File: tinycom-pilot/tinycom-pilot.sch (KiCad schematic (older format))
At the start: 31 parts, among them J1 MICRO_SD_HINGE, P1 CONN_02X08, P2 CONN_02X08, P3 USB_A, P4 USB_OTG, U1 SY8008BAAC, U2 SY8008BAAC, U3 SY8008BAAC, U4 RTL8723BS(ComboModule)

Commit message: pilot pic
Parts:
- removed C12: CP_Small, Capacitors_Elko_ThroughHole:Elko_vert_11.2x6.3mm_RM2.5_CopperClear, symbol CP_Small
- removed HDMI1: HDMI-SWM-19, tinycom:HDMI-SWM-19, symbol HDMI-SWM-19
- removed P4: USB_OTG, tinycom:tc-USB_Micro-B, symbol USB_OTG
- removed U4: RTL8723BS(ComboModule), tinycom:RL-SM02BD(RTL8723BS), symbol RTL8723BS(ComboModule)
- added U4: conn-3x10, tinycom:Pin_Header_Angled_3x10, symbol conn-3x10
- added U5: STM32-48PIN, Housings_QFP:LQFP-48_7x7mm_Pitch0.5mm, symbol STM32-48PIN
- added U6: MPU6050, Housings_DFN_QFN:QFN-24-1EP_4x4mm_Pitch0.5mm, symbol MPU6050
- added U7: MS6511, tinycom:ms5611, symbol MS6511
- C11: footprint Capacitors_Elko_ThroughHole:Elko_vert_11.2x6.3mm_RM2.5_CopperClear -> Capacitors_Tantalum_SMD:TantalC_SizeT_EIA-3528
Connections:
- wire segments 118 -> 108
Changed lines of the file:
@@
 LIBS:tinycom
 LIBS:hdmi-swm-19
-LIBS:tinycom-wifi-cache
+LIBS:conn-3x10
+LIBS:tinycom-pilot-cache
 EELAYER 25 0
 EELAYER END
@@
 $EndComp
 $Comp
-L +5V #PWR14
-U 1 1 562DA8F7
-P 5250 4200
-F 0 "#PWR14" H 5250 4050 50  0001 C CNN
-F 1 "+5V" H 5250 4340 50  0000 C CNN
-F 2 "" H 5250 4200 60  0000 C CNN
-F 3 "" H 5250 4200 60  0000 C CNN
-	1    5250 4200
-	1    0    0    -1
-$EndComp
-$Comp
-L GND #PWR15
-U 1 1 562DA928
-P 5250 4600
-F 0 "#PWR15" H 5250 4350 50  0001 C CNN
-F 1 "GND" H 5250 4450 50  0000 C CNN
-F 2 "" H 5250 4600 60  0000 C CNN
-F 3 "" H 5250 4600 60  0000 C CNN
-	1    5250 4600
-	1    0    0    -1
-$EndComp
-Text GLabel 5450 4350 0    60   Input ~ 0
-UDM0
-Text GLabel 5450 4450 0    60   Input ~ 0
-UDP0
-$Comp
-L +5V #PWR16
+L +5V #PWR01
 U 1 1 562DAC42
 P 5300 5050
-F 0 "#PWR16" H 5300 4900 50  0001 C CNN
+F 0 "#PWR01" H 5300 4900 50  0001 C CNN
 F 1 "+5V" H 5300 5190 50  0000 C CNN
 F 2 "" H 5300 5050 60  0000 C CNN
@@
 $EndComp
 $Comp
-L GND #PWR17
+L GND #PWR02
 U 1 1 562DAC77
 P 5300 5500
-F 0 "#PWR17" H 5300 5250 50  0001 C CNN
+F 0 "#PWR02" H 5300 5250 50  0001 C CNN
 F 1 "GND" H 5300 5350 50  0000 C CNN
 F 2 "" H 5300 5500 60  0000 C CNN
@@
 UDP1
 $Comp
-L GND #PWR5
+L GND #PWR03
 U 1 1 562DAF0B
 P 1350 1750
-F 0 "#PWR5" H 1350 1500 50  0001 C CNN
+F 0 "#PWR03" H 1350 1500 50  0001 C CNN
 F 1 "GND" H 1350 1600 50  0000 C CNN
 F 2 "" H 1350 1750 60  0000 C CNN
@@
 $EndComp
 $Comp
-L +5V #PWR3
+L +5V #PWR04
 U 1 1 562DAF87
 P 1250 1350
-F 0 "#PWR3" H 1250 1200 50  0001 C CNN
+F 0 "#PWR04" H 1250 1200 50  0001 C CNN
 F 1 "+5V" H 1250 1490 50  0000 C CNN
 F 2 "" H 1250 1350 60  0000 C CNN
@@
 $EndComp
 $Comp
-L +5V #PWR1
+L +5V #PWR05
 U 1 1 562DB0A5
 P 1150 2550
-F 0 "#PWR1" H 1150 2400 50  0001 C CNN
+F 0 "#PWR05" H 1150 2400 50  0001 C CNN
 F 1 "+5V" H 1150 2690 50  0000 C CNN
 F 2 "" H 1150 2550 60  0000 C CNN
@@
 $EndComp
 $Comp
-L GND #PWR6
+L GND #PWR06
 U 1 1 562DB1B7
 P 1350 2900
-F 0 "#PWR6" H 1350 2650 50  0001 C CNN
+F 0 "#PWR06" H 1350 2650 50  0001 C CNN
 F 1 "GND" H 1350 2750 50  0000 C CNN
 F 2 "" H 1350 2900 60  0000 C CNN
@@
 $EndComp
 $Comp
-L +5V #PWR2
+L +5V #PWR07
 U 1 1 562DB2B7
 P 1150 3800
-F 0 "#PWR2" H 1150 3650 50  0001 C CNN
+F 0 "#PWR07" H 1150 3650 50  0001 C CNN
 F 1 "+5V" H 1150 3940 50  0000 C CNN
 F 2 "" H 1150 3800 60  0000 C CNN
@@
 $EndComp
 $Comp
-L GND #PWR4
+L GND #PWR08
 U 1 1 562DB346
 P 1300 4150
-F 0 "#PWR4" H 1300 3900 50  0001 C CNN
+F 0 "#PWR08" H 1300 3900 50  0001 C CNN
 F 1 "GND" H 1300 4000 50  0000 C CNN
 F 2 "" H 1300 4150 60  0000 C CNN
@@
 VCC_15
 $Comp
-L GND #PWR19
+L GND #PWR09
 U 1 1 562DAEC4
 P 7450 2400
-F 0 "#PWR19" H 7450 2150 50  0001 C CNN
+F 0 "#PWR09" H 7450 2150 50  0001 C CNN
 F 1 "GND" H 7450 2250 50  0000 C CNN
 F 2 "" H 7450 2400 60  0000 C CNN
@@
 $EndComp
 $Comp
-L GND #PWR21
+L GND #PWR010
 U 1 1 562DA997
 P 8650 2450
-F 0 "#PWR21" H 8650 2200 50  0001 C CNN
+F 0 "#PWR010" H 8650 2200 50  0001 C CNN
 F 1 "GND" H 8650 2300 50  0000 C CNN
 F 2 "" H 8650 2450 60  0000 C CNN
@@
 SDC0_D1
 $Comp
-L GND #PWR20
+L GND #PWR011
 U 1 1 562DAEE9
 P 7450 4950
-F 0 "#PWR20" H 7450 4700 50  0001 C CNN
+F 0 "#PWR011" H 7450 4700 50  0001 C CNN
 F 1 "GND" H 7450 4800 50  0000 C CNN
 F 2 "" H 7450 4950 60  0000 C CNN
@@
 $EndComp
 $Comp
-L GND #PWR22
+L GND #PWR012
 U 1 1 562DAF47
 P 9050 5450
-F 0 "#PWR22" H 9050 5200 50  0001 C CNN
+F 0 "#PWR012" H 9050 5200 50  0001 C CNN
 F 1 "GND" H 9050 5300 50  0000 C CNN
 F 2 "" H 9050 5450 60  0000 C CNN
@@
 $EndComp
 $Comp
-L +3.3V #PWR18
+L +3.3V #PWR013
 U 1 1 562DB369
 P 7300 4000
-F 0 "#PWR18" H 7300 3850 50  0001 C CNN
+F 0 "#PWR013" H 7300 3850 50  0001 C CNN
 F 1 "+3.3V" H 7300 4140 50  0000 C CNN
 F 2 "" H 7300 4000 60  0000 C CNN
@@
 $EndComp
 $Comp
-L GND #PWR9
+L GND #PWR014
 U 1 1 562DB89F
 P 3250 2000
-F 0 "#PWR9" H 3250 1750 50  0001 C CNN
+F 0 "#PWR014" H 3250 1750 50  0001 C CNN
 F 1 "GND" H 3250 1850 50  0000 C CNN
 F 2 "" H 3250 2000 60  0000 C CNN
@@
 $EndComp
 $Comp
-L +3.3V #PWR10
+L +3.3V #PWR015
 U 1 1 562DBC47
 P 3600 1350
-F 0 "#PWR10" H 3600 1200 50  0001 C CNN
+F 0 "#PWR015" H 3600 1200 50  0001 C CNN
 F 1 "+3.3V" H 3600 1490 50  0000 C CNN
 F 2 "" H 3600 1350 60  0000 C CNN
@@
 $EndComp
 $Comp
-L GND #PWR8
+L GND #PWR016
 U 1 1 562F8BF0
 P 3150 3150
-F 0 "#PWR8" H 3150 2900 50  0001 C CNN
+F 0 "#PWR016" H 3150 2900 50  0001 C CNN
 F 1 "GND" H 3150 3000 50  0000 C CNN
 F 2 "" H 3150 3150 60  0000 C CNN
@@
 $EndComp
 $Comp
-L GND #PWR7
+L GND #PWR017
 U 1 1 562F9FD4
 P 3100 4550
-F 0 "#PWR7" H 3100 4300 50  0001 C CNN
+F 0 "#PWR017" H 3100 4300 50  0001 C CNN
 F 1 "GND" H 3100 4400 50  0000 C CNN
 F 2 "" H 3100 4550 60  0000 C CNN
@@
 $EndComp
 $Comp
-L GND #PWR11
+L GND #PWR018
 U 1 1 56336272
 P 4400 1900
-F 0 "#PWR11" H 4400 1650 50  0001 C CNN
+F 0 "#PWR018" H 4400 1650 50  0001 C CNN
 F 1 "GND" H 4400 1750 50  0000 C CNN
 F 2 "" H 4400 1900 60  0000 C CNN
@@
 $EndComp
 $Comp
-L GND #PWR12
-U 1 1 5634B03F
-P 4900 4550
-F 0 "#PWR12" H 4900 4300 50  0001 C CNN
-F 1 "GND" H 4900 4400 50  0000 C CNN
-F 2 "" H 4900 4550 60  0000 C CNN
-F 3 "" H 4900 4550 60  0000 C CNN
-	1    4900 4550
-	1    0    0    -1
-$EndComp
-$Comp
-L GND #PWR13
+L GND #PWR019
 U 1 1 5634B0B0
 P 4900 5400
-F 0 "#PWR13" H 4900 5150 50  0001 C CNN
+F 0 "#PWR019" H 4900 5150 50  0001 C CNN
 F 1 "GND" H 4900 5250 50  0000 C CNN
 F 2 "" H 4900 5400 60  0000 C CNN
 F 3 "" H 4900 5400 60  0000 C CNN
 	1    4900 5400
-	1    0    0    -1
-$EndComp
-$Comp
-L CP_Small C11
-U 1 1 5634BEB9
-P 4600 5250
-F 0 "C11" H 4610 5320 50  0000 L CNN
-F 1 "CP_Small" H 4610 5170 50  0000 L CNN
-F 2 "Capacitors_Elko_ThroughHole:Elko_vert_11.2x6.3mm_RM2.5_CopperClear" H 4600 5250 60  0001 C CNN
-F 3 "" H 4600 5250 60  0000 C CNN
-	1    4600 5250
-	1    0    0    -1
-$EndComp
-$Comp
-L CP_Small C12
-U 1 1 5634C85E
-P 4650 4400
-F 0 "C12" H 4660 4470 50  0000 L CNN
-F 1 "CP_Small" H 4660 4320 50  0000 L CNN
-F 2 "Capacitors_Elko_ThroughHole:Elko_vert_11.2x6.3mm_RM2.5_CopperClear" H 4650 4400 60  0001 C CNN
-F 3 "" H 4650 4400 60  0000 C CNN
-	1    4650 4400
 	1    0    0    -1
 $EndComp
@@
 NoConn ~ 6800 2550
 NoConn ~ 6800 2650
-$Comp
-L USB_OTG P4
-U 1 1 565013FA
-P 5750 4450
-F 0 "P4" H 6075 4325 50  0000 C CNN
-F 1 "USB_OTG" H 5750 4650 50  0000 C CNN
-F 2 "tinycom:tc-USB_Micro-B" V 5700 4350 60  0000 C CNN
-F 3 "" V 5700 4350 60  0000 C CNN
-	1    5750 4450
-	0    1    1    0
-$EndComp
-Wire Wire Line
-	4650 4250 5450 4250
-Wire Wire Line
-	5250 4250 5250 4200
-Wire Wire Line
-	5450 4550 5250 4550
-Wire Wire Line
-	5250 4550 5250 4600
 Wire Wire Line
 	4600 5100 5450 5100
@@
 	4900 5350 4900 5400
 Wire Wire Line
-	4900 4500 4900 4550
-Connection ~ 5250 4250
-Wire Wire Line
-	4650 4250 4650 4300
-Wire Wire Line
-	4650 4500 4900 4500
-Wire Wire Line
 	4600 5100 4600 5150
 Wire Wire Line
@@
 Wire Wire Line
 	7200 4850 7450 4850
-Wire Wire Line
-	5450 4650 5350 4650
-Wire Wire Line
-	5350 4550 5350 4850
-Connection ~ 5350 4550
-Wire Wire Line
-	5350 4850 5850 4850
-Connection ~ 5350 4650
-$Comp
-L RTL8723BS(ComboModule) U4
-U 1 1 56591901
-P 2000 6200
-F 0 "U4" H 1600 7575 60  0000 C CNN
-F 1 "RTL8723BS(ComboModule)" H 2000 4825 60  0000 C CNN
-F 2 "tinycom:RL-SM02BD(RTL8723BS)" H 2000 6000 60  0000 C CNN
-F 3 "" H 2000 6000 60  0000 C CNN
-	1    2000 6200
-	1    0    0    -1
-$EndComp
 Wire Wire Line
 	7950 3950 7950 4750
@@
 	8250 3850 8250 4000
 $Comp
-L HDMI-SWM-19 HDMI1
-U 1 1 56591D96
-P 3450 6150
-F 0 "HDMI1" H 3550 7150 50  0000 L BNN
-F 1 "HDMI-SWM-19" H 3550 5050 50  0000 L BNN
-F 2 "tinycom:HDMI-SWM-19" H 3480 6300 20  0001 C CNN
-F 3 "" H 3450 6150 60  0000 C CNN
-	1    3450 6150
-	1    0    0    -1
-$EndComp
+L conn-3x10 U4
+U 1 1 56594134
+P 1750 5350
+F 0 "U4" H 1750 5350 60  0000 C CNN
+F 1 "conn-3x10" H 1750 5350 60  0000 C CNN
+F 2 "tinycom:Pin_Header_Angled_3x10" H 1750 5350 60  0000 C CNN
+F 3 "" H 1750 5350 60  0000 C CNN
+	1    1750 5350
+	1    0    0    -1
+$EndComp
+$Comp
+L STM32-48PIN U5
+U 1 1 5659585F
+P 3350 7350
+F 0 "U5" H 2350 9100 60  0000 C CNN
+F 1 "STM32-48PIN" H 2600 5550 60  0000 C CNN
+F 2 "Housings_QFP:LQFP-48_7x7mm_Pitch0.5mm" H 3350 7350 60  0000 C CNN
+F 3 "" H 3350 7350 60  0000 C CNN
+	1    3350 7350
+	1    0    0    -1
+$EndComp
+$Comp
+L CP_Small C11
+U 1 1 5634BEB9
+P 4600 5250
+F 0 "C11" H 4610 5320 50  0000 L CNN
+F 1 "CP_Small" H 4610 5170 50  0000 L CNN
+F 2 "Capacitors_Tantalum_SMD:TantalC_SizeT_EIA-3528" H 4600 5250 60  0001 C CNN
+F 3 "" H 4600 5250 60  0000 C CNN
+	1    4600 5250
+	1    0    0    -1
+$EndComp
+$Comp
+L MPU6050 U6
+U 1 1 5659749B
+P 8600 1350
+F 0 "U6" H 8550 1450 60  0000 C CNN
+F 1 "MPU6050" H 8550 1450 60  0000 C CNN
+F 2 "Housings_DFN_QFN:QFN-24-1EP_4x4mm_Pitch0.5mm" H 8550 1450 60  0000 C CNN
+F 3 "" H 8550 1450 60  0000 C CNN
+	1    8600 1350
+	1    0    0    -1
+$EndComp
+$Comp
+L MS6511 U7
+U 1 1 56597816
+P 10000 1050
+F 0 "U7" H 10000 1050 60  0000 C CNN
+F 1 "MS6511" H 10000 1050 60  0000 C CNN
+F 2 "tinycom:ms5611" H 10000 1050 60  0000 C CNN
+F 3 "" H 10000 1050 60  0000 C CNN
+	1    10000 1050
+	1    0    0    -1
+$EndComp

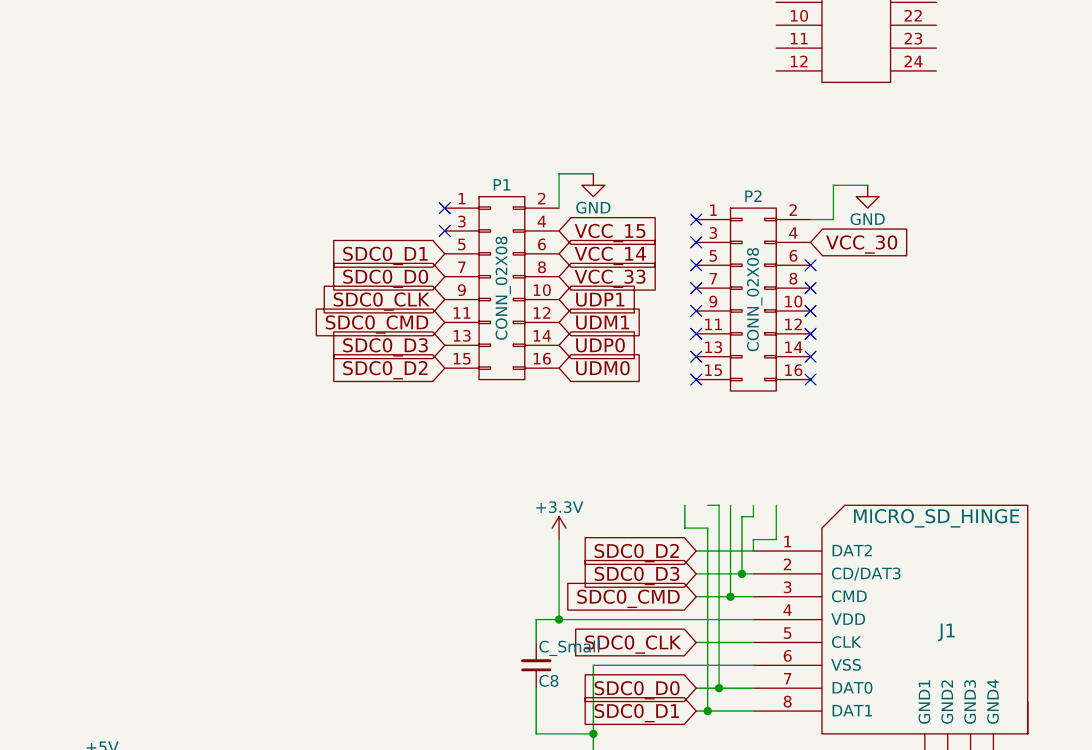
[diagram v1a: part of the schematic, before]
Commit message: change connectors
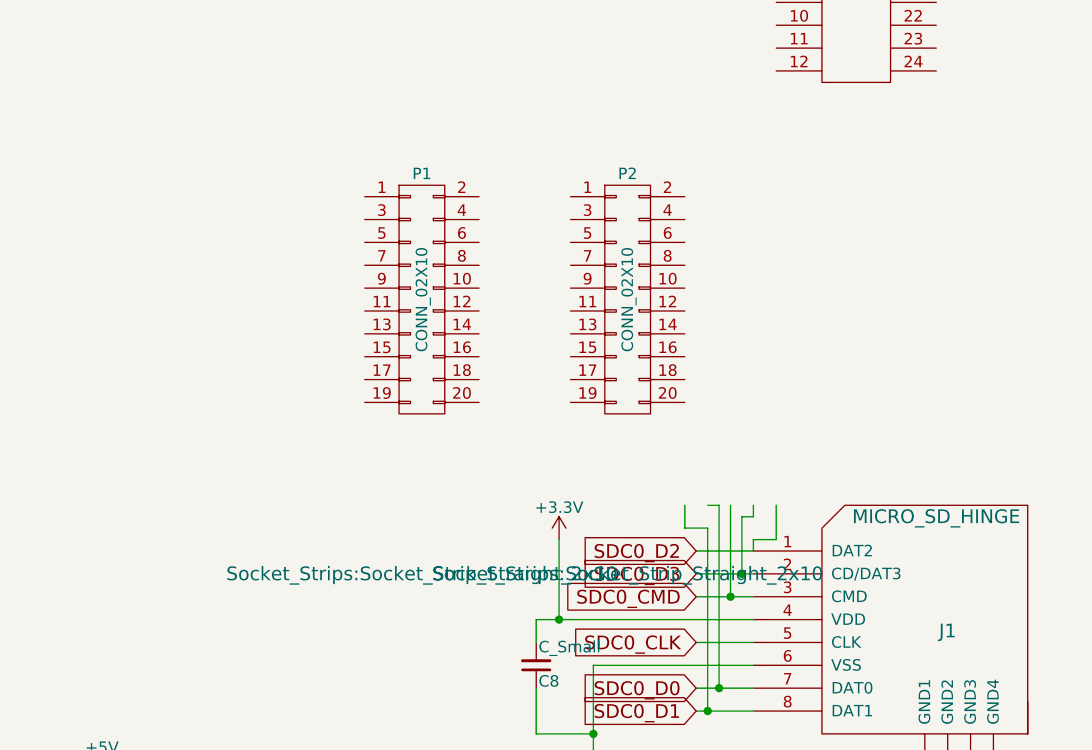
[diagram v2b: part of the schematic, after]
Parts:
- removed P1, P2: CONN_02X08, Socket_Strips:Socket_Strip_Straight_2x08, symbol CONN_02X08
- added P1, P2: CONN_02X10, Socket_Strips:Socket_Strip_Straight_2x10, symbol CONN_02X10
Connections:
- net labels removed: UDM0, UDP0
- wire segments 108 -> 103
- no-connect marks 16 -> 0
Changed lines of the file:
@@
 $EndDescr
-$Comp
-L CONN_02X08 P1
-U 1 1 562BA4D4
-P 7050 2900
-F 0 "P1" H 7050 3350 50  0000 C CNN
-F 1 "CONN_02X08" V 7050 2900 50  0000 C CNN
-F 2 "Socket_Strips:Socket_Strip_Straight_2x08" H 7050 1700 60  0001 C CNN
-F 3 "" H 7050 1700 60  0000 C CNN
-	1    7050 2900
-	1    0    0    -1
-$EndComp
-$Comp
-L CONN_02X08 P2
-U 1 1 562BA547
-P 8150 2950
-F 0 "P2" H 8150 3400 50  0000 C CNN
-F 1 "CONN_02X08" V 8150 2950 50  0000 C CNN
-F 2 "Socket_Strips:Socket_Strip_Straight_2x08" H 8150 1750 60  0001 C CNN
-F 3 "" H 8150 1750 60  0000 C CNN
-	1    8150 2950
-	1    0    0    -1
-$EndComp
 $Comp
 L USB_A P3
@@
 $EndComp
 $Comp
-L +5V #PWR01
+L +5V #PWR13
 U 1 1 562DAC42
 P 5300 5050
-F 0 "#PWR01" H 5300 4900 50  0001 C CNN
+F 0 "#PWR13" H 5300 4900 50  0001 C CNN
 F 1 "+5V" H 5300 5190 50  0000 C CNN
 F 2 "" H 5300 5050 60  0000 C CNN
@@
 $EndComp
 $Comp
-L GND #PWR02
+L GND #PWR14
 U 1 1 562DAC77
 P 5300 5500
-F 0 "#PWR02" H 5300 5250 50  0001 C CNN
+F 0 "#PWR14" H 5300 5250 50  0001 C CNN
 F 1 "GND" H 5300 5350 50  0000 C CNN
 F 2 "" H 5300 5500 60  0000 C CNN
@@
 UDP1
 $Comp
-L GND #PWR03
+L GND #PWR5
 U 1 1 562DAF0B
 P 1350 1750
-F 0 "#PWR03" H 1350 1500 50  0001 C CNN
+F 0 "#PWR5" H 1350 1500 50  0001 C CNN
 F 1 "GND" H 1350 1600 50  0000 C CNN
 F 2 "" H 1350 1750 60  0000 C CNN
@@
 $EndComp
 $Comp
-L +5V #PWR04
+L +5V #PWR3
 U 1 1 562DAF87
 P 1250 1350
-F 0 "#PWR04" H 1250 1200 50  0001 C CNN
+F 0 "#PWR3" H 1250 1200 50  0001 C CNN
 F 1 "+5V" H 1250 1490 50  0000 C CNN
 F 2 "" H 1250 1350 60  0000 C CNN
@@
 $EndComp
 $Comp
-L +5V #PWR05
+L +5V #PWR1
 U 1 1 562DB0A5
 P 1150 2550
-F 0 "#PWR05" H 1150 2400 50  0001 C CNN
+F 0 "#PWR1" H 1150 2400 50  0001 C CNN
 F 1 "+5V" H 1150 2690 50  0000 C CNN
 F 2 "" H 1150 2550 60  0000 C CNN
@@
 $EndComp
 $Comp
-L GND #PWR06
+L GND #PWR6
 U 1 1 562DB1B7
 P 1350 2900
-F 0 "#PWR06" H 1350 2650 50  0001 C CNN
+F 0 "#PWR6" H 1350 2650 50  0001 C CNN
 F 1 "GND" H 1350 2750 50  0000 C CNN
 F 2 "" H 1350 2900 60  0000 C CNN
@@
 $EndComp
 $Comp
-L +5V #PWR07
+L +5V #PWR2
 U 1 1 562DB2B7
 P 1150 3800
-F 0 "#PWR07" H 1150 3650 50  0001 C CNN
+F 0 "#PWR2" H 1150 3650 50  0001 C CNN
 F 1 "+5V" H 1150 3940 50  0000 C CNN
 F 2 "" H 1150 3800 60  0000 C CNN
@@
 $EndComp
 $Comp
-L GND #PWR08
+L GND #PWR4
 U 1 1 562DB346
 P 1300 4150
-F 0 "#PWR08" H 1300 3900 50  0001 C CNN
+F 0 "#PWR4" H 1300 3900 50  0001 C CNN
 F 1 "GND" H 1300 4000 50  0000 C CNN
 F 2 "" H 1300 4150 60  0000 C CNN
@@
 	1    0    0    -1
 $EndComp
-Text GLabel 7300 3250 2    60   Input ~ 0
-UDM0
-Text GLabel 7300 3150 2    60   Input ~ 0
-UDP0
-Text GLabel 7300 3050 2    60   Input ~ 0
-UDM1
-Text GLabel 7300 2950 2    60   Input ~ 0
-UDP1
-Text GLabel 6800 3250 0    60   Input ~ 0
-SDC0_D2
-Text GLabel 6800 3150 0    60   Input ~ 0
-SDC0_D3
-Text GLabel 6800 3050 0    60   Input ~ 0
-SDC0_CMD
-Text GLabel 6800 2950 0    60   Input ~ 0
-SDC0_CLK
-Text GLabel 6800 2850 0    60   Input ~ 0
-SDC0_D0
-Text GLabel 6800 2750 0    60   Input ~ 0
-SDC0_D1
-Text GLabel 7300 2850 2    60   Input ~ 0
-VCC_33
-Text GLabel 7300 2750 2    60   Input ~ 0
-VCC_14
-Text GLabel 7300 2650 2    60   Input ~ 0
-VCC_15
-$Comp
-L GND #PWR09
-U 1 1 562DAEC4
-P 7450 2400
-F 0 "#PWR09" H 7450 2150 50  0001 C CNN
-F 1 "GND" H 7450 2250 50  0000 C CNN
-F 2 "" H 7450 2400 60  0000 C CNN
-F 3 "" H 7450 2400 60  0000 C CNN
-	1    7450 2400
-	1    0    0    -1
-$EndComp
-$Comp
-L GND #PWR010
-U 1 1 562DA997
-P 8650 2450
-F 0 "#PWR010" H 8650 2200 50  0001 C CNN
-F 1 "GND" H 8650 2300 50  0000 C CNN
-F 2 "" H 8650 2450 60  0000 C CNN
-F 3 "" H 8650 2450 60  0000 C CNN
-	1    8650 2450
-	1    0    0    -1
-$EndComp
-Text GLabel 8400 2700 2    60   Input ~ 0
-VCC_30
 Text GLabel 7900 4050 0    60   Input ~ 0
 SDC0_D2
@@
 SDC0_D1
 $Comp
-L GND #PWR011
+L GND #PWR16
 U 1 1 562DAEE9
 P 7450 4950
-F 0 "#PWR011" H 7450 4700 50  0001 C CNN
+F 0 "#PWR16" H 7450 4700 50  0001 C CNN
 F 1 "GND" H 7450 4800 50  0000 C CNN
 F 2 "" H 7450 4950 60  0000 C CNN
@@
 $EndComp
 $Comp
-L GND #PWR012
+L GND #PWR17
 U 1 1 562DAF47
 P 9050 5450
-F 0 "#PWR012" H 9050 5200 50  0001 C CNN
+F 0 "#PWR17" H 9050 5200 50  0001 C CNN
 F 1 "GND" H 9050 5300 50  0000 C CNN
 F 2 "" H 9050 5450 60  0000 C CNN
@@
 $EndComp
 $Comp
-L +3.3V #PWR013
+L +3.3V #PWR15
 U 1 1 562DB369
 P 7300 4000
-F 0 "#PWR013" H 7300 3850 50  0001 C CNN
+F 0 "#PWR15" H 7300 3850 50  0001 C CNN
 F 1 "+3.3V" H 7300 4140 50  0000 C CNN
 F 2 "" H 7300 4000 60  0000 C CNN
@@
 $EndComp
 $Comp
-L GND #PWR014
+L GND #PWR9
 U 1 1 562DB89F
 P 3250 2000
-F 0 "#PWR014" H 3250 1750 50  0001 C CNN
+F 0 "#PWR9" H 3250 1750 50  0001 C CNN
 F 1 "GND" H 3250 1850 50  0000 C CNN
 F 2 "" H 3250 2000 60  0000 C CNN
@@
 $EndComp
 $Comp
-L +3.3V #PWR015
+L +3.3V #PWR10
 U 1 1 562DBC47
 P 3600 1350
-F 0 "#PWR015" H 3600 1200 50  0001 C CNN
+F 0 "#PWR10" H 3600 1200 50  0001 C CNN
 F 1 "+3.3V" H 3600 1490 50  0000 C CNN
 F 2 "" H 3600 1350 60  0000 C CNN
@@
 $EndComp
 $Comp
-L GND #PWR016
+L GND #PWR8
 U 1 1 562F8BF0
 P 3150 3150
-F 0 "#PWR016" H 3150 2900 50  0001 C CNN
+F 0 "#PWR8" H 3150 2900 50  0001 C CNN
 F 1 "GND" H 3150 3000 50  0000 C CNN
 F 2 "" H 3150 3150 60  0000 C CNN
@@
 $EndComp
 $Comp
-L GND #PWR017
+L GND #PWR7
 U 1 1 562F9FD4
 P 3100 4550
-F 0 "#PWR017" H 3100 4300 50  0001 C CNN
+F 0 "#PWR7" H 3100 4300 50  0001 C CNN
 F 1 "GND" H 3100 4400 50  0000 C CNN
 F 2 "" H 3100 4550 60  0000 C CNN
@@
 $EndComp
 $Comp
-L GND #PWR018
+L GND #PWR11
 U 1 1 56336272
 P 4400 1900
-F 0 "#PWR018" H 4400 1650 50  0001 C CNN
+F 0 "#PWR11" H 4400 1650 50  0001 C CNN
 F 1 "GND" H 4400 1750 50  0000 C CNN
 F 2 "" H 4400 1900 60  0000 C CNN
@@
 $EndComp
 $Comp
-L GND #PWR019
+L GND #PWR12
 U 1 1 5634B0B0
 P 4900 5400
-F 0 "#PWR019" H 4900 5150 50  0001 C CNN
+F 0 "#PWR12" H 4900 5150 50  0001 C CNN
 F 1 "GND" H 4900 5250 50  0000 C CNN
 F 2 "" H 4900 5400 60  0000 C CNN
@@
 	1    0    0    -1
 $EndComp
-NoConn ~ 8400 2800
-NoConn ~ 8400 2900
-NoConn ~ 8400 3000
-NoConn ~ 8400 3100
-NoConn ~ 8400 3200
-NoConn ~ 8400 3300
-NoConn ~ 7900 2600
-NoConn ~ 7900 2700
-NoConn ~ 7900 2800
-NoConn ~ 7900 2900
-NoConn ~ 7900 3000
-NoConn ~ 7900 3100
-NoConn ~ 7900 3200
-NoConn ~ 7900 3300
-NoConn ~ 6800 2550
-NoConn ~ 6800 2650
 Wire Wire Line
 	4600 5100 5450 5100
@@
 	1350 2750 1350 2650
 Connection ~ 1350 2650
-Wire Wire Line
-	7300 2550 7300 2400
-Wire Wire Line
-	7300 2400 7450 2400
-Wire Wire Line
-	8400 2600 8500 2600
-Wire Wire Line
-	8500 2600 8500 2450
-Wire Wire Line
-	8500 2450 8650 2450
 Wire Wire Line
 	8150 4550 7450 4550
@@
 	1    0    0    -1
 $EndComp
+$Comp
+L CONN_02X10 P1
+U 1 1 565A983B
+P 6700 2950
+F 0 "P1" H 6700 3500 50  0000 C CNN
+F 1 "CONN_02X10" V 6700 2950 50  0000 C CNN
+F 2 "Socket_Strips:Socket_Strip_Straight_2x10" H 6700 1750 60  0000 C CNN
+F 3 "" H 6700 1750 60  0000 C CNN
+	1    6700 2950
+	1    0    0    -1
+$EndComp
+$Comp
+L CONN_02X10 P2
+U 1 1 565A9C25
+P 7600 2950
+F 0 "P2" H 7600 3500 50  0000 C CNN
+F 1 "CONN_02X10" V 7600 2950 50  0000 C CNN
+F 2 "Socket_Strips:Socket_Strip_Straight_2x10" H 7600 1750 60  0000 C CNN
+F 3 "" H 7600 1750 60  0000 C CNN
+	1    7600 2950
+	1    0    0    -1
+$EndComp
